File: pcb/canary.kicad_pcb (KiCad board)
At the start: 2 copper layers, 65 x 56 mm, 26 parts, among them J1 Raspberry_Pi_4, J2 Conn_01x02_Pin, U1 TMP119AIYBGR, U2 BMP388, U3 SGP40-D-R4, U4 SHT4x, U5 CAT24C32WI-GT3

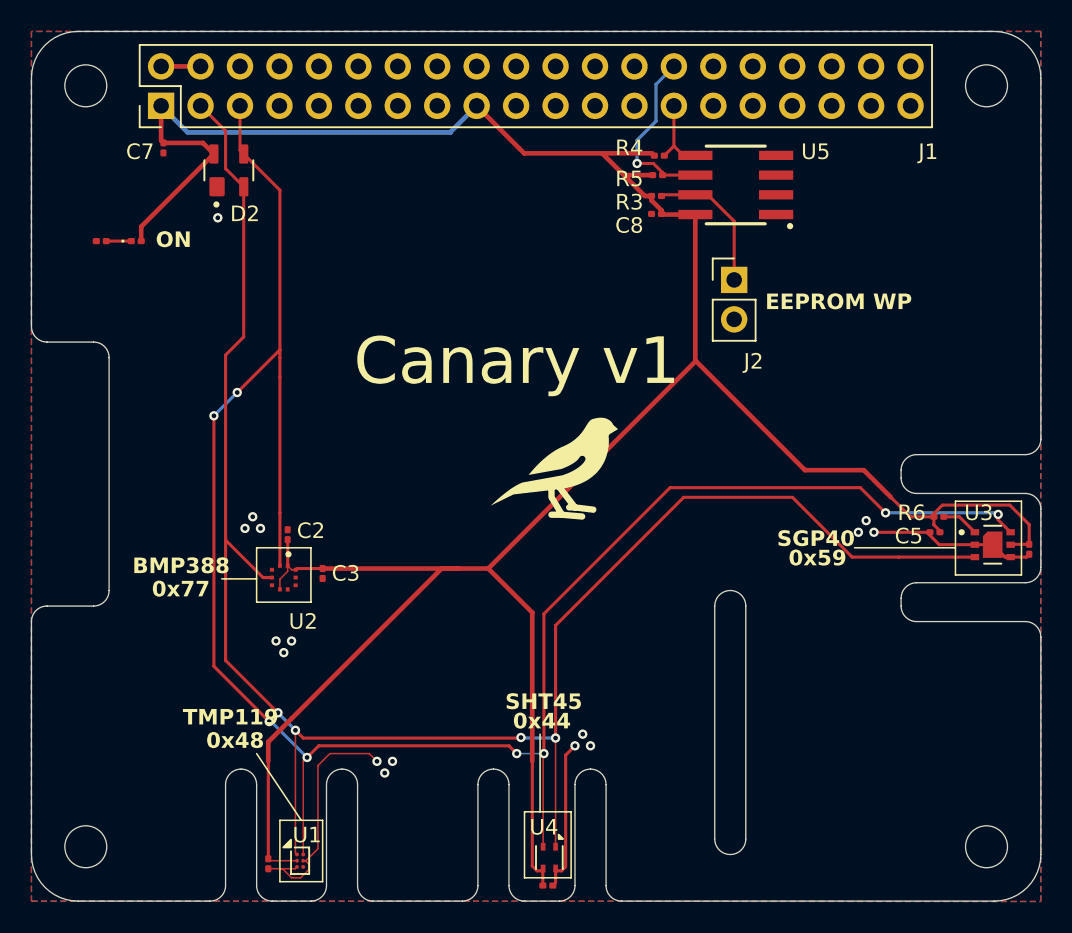
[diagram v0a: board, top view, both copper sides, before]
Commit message: complete pcb design (v1 fab), implement backend mqtt service
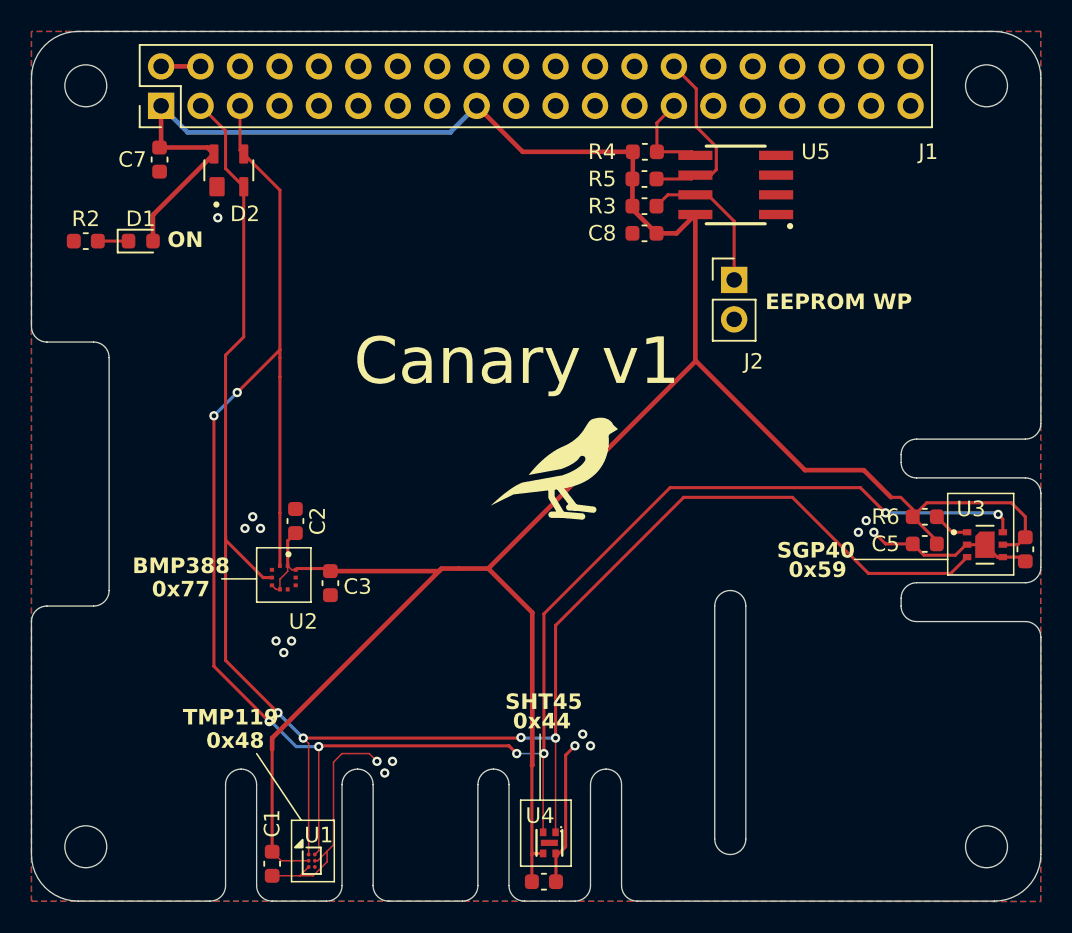
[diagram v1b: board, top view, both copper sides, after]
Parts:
- C1, C2, C3, C4, C5, C6, C7, C8: footprint Capacitor_SMD:C_0201_0603Metric -> Capacitor_SMD:C_0603_1608Metric
- D1: footprint LED_SMD:LED_0201_0603Metric -> LED_SMD:LED_0603_1608Metric
- R2, R3, R4, R5, R6: footprint Resistor_SMD:R_0201_0603Metric -> Capacitor_SMD:C_0603_1608Metric
- U4: footprint Sensor_Humidity:Sensirion_DFN-4_1.5x1.5mm_P0.8mm_SHT4x_NoCentralPad -> My_Footprints:DFN-4_L1.5-W1.5-P0.8-TL-EP
- moved C8 1.47 mm to (189.5, 88.0)
- moved R3 1.01 mm to (189.5, 86.2)
- moved C2 1.01 mm to (167.0, 106.5)
- moved R2 1.00 mm to (153.5, 88.5)
- moved C5 1.00 mm to (207.5, 108.0)
- moved R4 0.96 mm to (189.5, 82.8)
- moved U4 0.95 mm to (183.4, 127.2)
- moved R6 0.91 mm to (207.5, 106.2)
- moved R5 0.88 mm to (189.5, 84.5)
- moved C3 0.80 mm to (169.2, 110.5)
- moved C7 0.79 mm to (158.2, 83.2)
- moved U1 0.75 mm to (168.1, 128.4)
- moved U3 0.50 mm to (211.4, 108.0)
- moved C6 0.35 mm to (183.0, 129.8)
- moved D1 0.29 mm to (157.0, 88.5)
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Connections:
- U2 pad 5: GND -> +3.3V
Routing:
- net SDA_0: track 5.10 -> 6.98 mm
- net SDA: track 119.4 -> 118.3 mm
- net SCL: track 133.3 -> 132.2 mm
- net +3.3V: track 181.7 -> 180.7 mm
- net GND: track 36.9 -> 36.3 mm
- net Net-(J2-Pin_1): track 9.20 -> 9.79 mm
- net SCL_0: track 11.4 -> 11.9 mm, vias 1 -> 0
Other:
- outline, holes or cut-outs redrawn
